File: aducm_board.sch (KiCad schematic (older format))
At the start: 34 parts, among them J1 Conn_02x04_Odd_Even, J4 USB_C_Receptacle_USB2.0, J5 Conn_02x25_Odd_Even, SW1 SW_Push, U1 aducm_355, Y1 32MHz

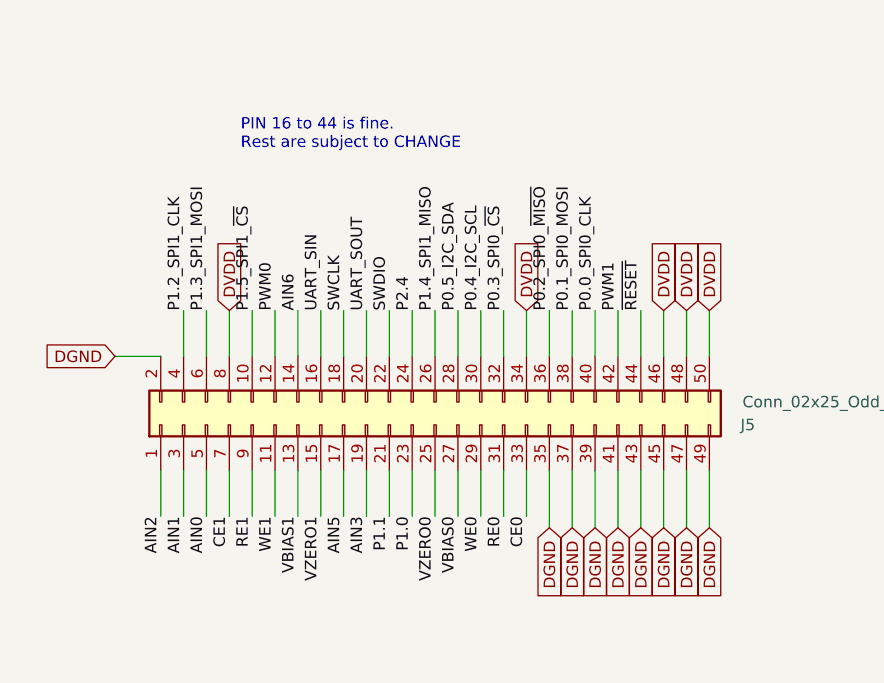
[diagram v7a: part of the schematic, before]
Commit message: routing right side of chip. changing the gpio connections
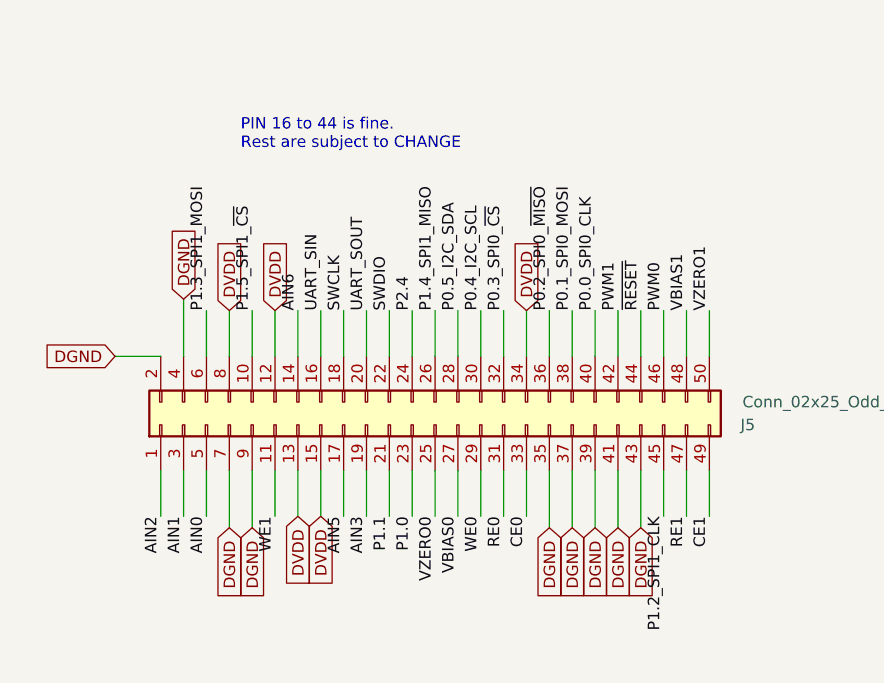
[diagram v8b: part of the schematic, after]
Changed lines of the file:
@@
 Text Label 2800 10000 3    50   ~ 0
 VZERO0
-Text Label 1900 10000 3    50   ~ 0
+Text Label 4000 10000 3    50   ~ 0
 CE1
-Text Label 2000 10000 3    50   ~ 0
+Text Label 3900 10000 3    50   ~ 0
 RE1
 Text Label 2100 10000 3    50   ~ 0
 WE1
-Text Label 2200 10000 3    50   ~ 0
+Text Label 3900 9100 1    50   ~ 0
 VBIAS1
-Text Label 2300 10000 3    50   ~ 0
+Text Label 4000 9100 1    50   ~ 0
 VZERO1
 Text Label 7500 3000 0    50   ~ 0
@@
 Text Label 2600 10000 3    50   ~ 0
 P1.1
-Text Label 1700 9100 1    50   ~ 0
+Text Label 3800 10000 3    50   ~ 0
 P1.2_SPI1_CLK
 Text Label 1800 9100 1    50   ~ 0
@@
 Text Label 2700 9100 1    50   ~ 0
 P2.4
-Text Label 2100 9100 1    50   ~ 0
+Text Label 3800 9100 1    50   ~ 0
 PWM0
 Text Label 3600 9100 1    50   ~ 0
@@
 	2800 10000 2800 9800
 Wire Wire Line
-	1900 10000 1900 9800
-Wire Wire Line
-	2000 9800 2000 10000
+	4000 10000 4000 9800
+Wire Wire Line
+	3900 9800 3900 10000
 Wire Wire Line
 	2100 10000 2100 9800
 Wire Wire Line
-	2200 9800 2200 10000
-Wire Wire Line
-	2300 10000 2300 9800
+	3900 9300 3900 9100
+Wire Wire Line
+	4000 9100 4000 9300
 Wire Wire Line
 	3500 9100 3500 9300
@@
 	3600 9300 3600 9100
 Wire Wire Line
-	2100 9100 2100 9300
+	3800 9100 3800 9300
 Wire Wire Line
 	2000 9300 2000 9100
@@
 	1800 9300 1800 9100
 Wire Wire Line
-	1700 9100 1700 9300
+	3800 10000 3800 9800
 Text GLabel 1900 9100 1    50   Input ~ 0
 DVDD
-Text GLabel 4000 10050 3    50   Input ~ 0
-DGND
-Wire Wire Line
-	4000 10050 4000 9800
-Text GLabel 3900 10050 3    50   Input ~ 0
-DGND
-Text GLabel 3800 10050 3    50   Input ~ 0
-DGND
-Wire Wire Line
-	3900 9800 3900 10050
-Wire Wire Line
-	3800 9800 3800 10050
+Text GLabel 2000 10050 3    50   Input ~ 0
+DGND
+Wire Wire Line
+	2000 10050 2000 9800
+Text GLabel 1900 10050 3    50   Input ~ 0
+DGND
+Text GLabel 1700 9050 1    50   Input ~ 0
+DGND
+Wire Wire Line
+	1900 9800 1900 10050
+Wire Wire Line
+	1700 9300 1700 9050
 Wire Wire Line
 	1600 9800 1600 10000
@@
 Wire Wire Line
 	3600 10050 3600 9800
-Text GLabel 3800 9100 1    50   Input ~ 0
-DVDD
-Text GLabel 3900 9100 1    50   Input ~ 0
-DVDD
-Text GLabel 4000 9100 1    50   Input ~ 0
+Text GLabel 2100 9100 1    50   Input ~ 0
+DVDD
+Text GLabel 2300 10000 3    50   Input ~ 0
+DVDD
+Text GLabel 2200 10000 3    50   Input ~ 0
 DVDD
 Wire Wire Line
 	3700 9300 3700 9100
 Wire Wire Line
-	4000 9300 4000 9100
-Wire Wire Line
-	3900 9100 3900 9300
-Wire Wire Line
-	3800 9300 3800 9100
+	2200 9800 2200 10000
+Wire Wire Line
+	2300 10000 2300 9800
+Wire Wire Line
+	2100 9300 2100 9100
 Wire Wire Line
 	1900 9300 1900 9100
